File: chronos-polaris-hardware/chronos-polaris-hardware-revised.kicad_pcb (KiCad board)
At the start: 2 copper layers, 30 x 50 mm, 102 parts, among them J1 Conn_01x03_Pin, J2 Conn_01x03_Pin, J3 Conn_01x03_Pin, J4 Conn_01x03_Pin, J5 Conn_01x03_Pin, J6 Conn_01x04, J7 Conn_01x04, J8 Conn_01x02, J9 691417320006S, P1 WJ124-3_81-6P, Q1 US6K4TR, U1 TLV62130RGTR, U1 TPS62172DSGR, U10 MSK12C02-HB, U11 TPS62172DSGR, U12 AP20P30Q, U14 FC-B1010RGBT-HG, U15 TYPE-C_14PLC-H10_0, U2 ESP32-S2-SOLO-2-N4, U3 BMI088, U4 BMP280, U4 TYPE-C_14PLC-H10_0, U5 TF_PUSH, U6 TLV62130RGTR, U6 TPS629206DRLR, U7 AP20P30Q, U8 2N7002KDW_72K, U9 BMP280

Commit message: added footprint
footprint added for rigel connector. now all we need is to draw traces, layout, then ready for submit to jlcpcb
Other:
- board size 30 x 50 mm -> 40 x 50 mm

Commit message: fix merge conflicts . - Rishik B.
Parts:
- added BUZ1: HNB09A03, polaris-fp:BUZ-TH_BD9.0-P5.00-D0.6-FD, F.Cu at (188.8, 86.7)
- added C1: 22uF, Capacitor_SMD:C_0603_1608Metric, B.Cu at (212.1, 85.9)
- added C10: 100nF, Capacitor_SMD:C_0402_1005Metric, B.Cu at (194.1, 65.4)
- added C11: 3.3nF, Capacitor_SMD:C_0402_1005Metric, B.Cu at (194.4, 92.0)
- added C12: 100nF, Capacitor_SMD:C_0402_1005Metric, B.Cu at (189.4, 90.9)
- added C2: 10uF, Capacitor_SMD:C_0805_2012Metric, B.Cu at (212.2, 83.9)
- added C3: 22uF, Capacitor_SMD:C_0603_1608Metric, B.Cu at (188.8, 82.4)
- added C4: 10uF, Capacitor_SMD:C_0805_2012Metric, B.Cu at (191.4, 92.4)
- added C5: 100nF, Capacitor_SMD:C_0402_1005Metric, B.Cu at (194.1, 68.7)
- added C6: 100nF, Capacitor_SMD:C_0402_1005Metric, F.Cu at (197.1, 84.4)
- added C7: 100nF, Capacitor_SMD:C_0402_1005Metric, F.Cu at (197.1, 85.4)
- added C8: 100nF, Capacitor_SMD:C_0402_1005Metric, F.Cu at (205.6, 89.4)
- added C9: 100nF, Capacitor_SMD:C_0402_1005Metric, F.Cu at (205.6, 83.9)
- added H1: MountingHole, MountingHole:MountingHole_3.2mm_M3_Pad, F.Cu at (212.1, 101.4)
- added H4: MountingHole, MountingHole:MountingHole_3.2mm_M3_Pad, F.Cu at (187.6, 65.9)
- added J1: Conn_01x03_Pin, Connector_PinHeader_2.54mm:PinHeader_1x03_P2.54mm_Vertical, F.Cu at (187.1, 72.4)
- added J2: Conn_01x03_Pin, Connector_PinHeader_2.54mm:PinHeader_1x03_P2.54mm_Vertical, F.Cu at (187.1, 75.0)
- added J3: Conn_01x03_Pin, Connector_PinHeader_2.54mm:PinHeader_1x03_P2.54mm_Vertical, F.Cu at (187.1, 77.6)
- added J4: Conn_01x03_Pin, Connector_PinHeader_2.54mm:PinHeader_1x03_P2.54mm_Vertical, F.Cu at (187.1, 80.2)
- added J5: Conn_01x03_Pin, Connector_PinHeader_2.54mm:PinHeader_1x03_P2.54mm_Vertical, F.Cu at (186.0, 97.6)
- added J6: Conn_01x04, Connector_PinHeader_2.54mm:PinHeader_1x04_P2.54mm_Vertical, F.Cu at (186.0, 100.2)
- added J7: Conn_01x04, Connector_PinHeader_2.54mm:PinHeader_1x04_P2.54mm_Vertical, F.Cu at (186.0, 94.9)
- added J8: Conn_01x02, Connector_PinHeader_2.54mm:PinHeader_1x02_P2.54mm_Vertical, F.Cu at (192.6, 64.4)
- added J9: 691417320006S, polaris-fp:691417320006S, F.Cu at (202.5, 119.4)
- added L1: 2.2uH, polaris-fp:IND-SMD_L3.0-W3.0, B.Cu at (207.8, 89.2)
- added L2: 2.2uH, polaris-fp:IND-SMD_L4.0-W4.0, B.Cu at (192.6, 84.2)
- added R1: 100k, Resistor_SMD:R_0603_1608Metric, B.Cu at (206.6, 85.5)
- added R10: 51, Resistor_SMD:R_0603_1608Metric, B.Cu at (191.2, 70.2)
- added R11: 100, Resistor_SMD:R_0603_1608Metric, F.Cu at (191.3, 69.7)
- added R12: 0603WAF5101T5E, polaris-fp:R0603, B.Cu at (185.9, 111.7)
- added R13: 0603WAF5101T5E, polaris-fp:R0603, B.Cu at (188.8, 111.7)
- added R14: 30k, Resistor_SMD:R_0603_1608Metric, B.Cu at (208.0, 110.7)
- added R15: 10k, Resistor_SMD:R_0603_1608Metric, B.Cu at (208.1, 113.4)
- added R16: 10k, Resistor_SMD:R_0603_1608Metric, B.Cu at (198.9, 110.4)
- added R17: 30k, Resistor_SMD:R_0603_1608Metric, B.Cu at (193.1, 113.9)
- added R18: 10k, Resistor_SMD:R_0603_1608Metric, B.Cu at (192.8, 110.4)
- added R19: 100k, Resistor_SMD:R_0603_1608Metric, B.Cu at (197.1, 86.4)
- added R2: 10k, Resistor_SMD:R_0603_1608Metric, B.Cu at (196.1, 99.0)
- added R20: 160k, Resistor_SMD:R_0603_1608Metric, B.Cu at (195.6, 86.4)
- added R21: 10k, Resistor_SMD:R_0603_1608Metric, B.Cu at (189.6, 86.7)
- added R22: 30k, Resistor_SMD:R_0603_1608Metric, B.Cu at (209.9, 79.6)
- added R23: 10k, Resistor_SMD:R_0603_1608Metric, B.Cu at (209.9, 77.8)
- added R3: 10k, Resistor_SMD:R_0603_1608Metric, B.Cu at (202.6, 100.9)
- added R4: 10k, Resistor_SMD:R_0603_1608Metric, B.Cu at (199.1, 100.9)
- added R5: 10k, Resistor_SMD:R_0603_1608Metric, B.Cu at (199.1, 106.7)
- added R6: 10k, Resistor_SMD:R_0603_1608Metric, B.Cu at (202.4, 110.4)
- added R7: 30k, Resistor_SMD:R_0603_1608Metric, B.Cu at (195.6, 89.6)
- added R8: 10k, Resistor_SMD:R_0603_1608Metric, B.Cu at (191.8, 68.7)
- added R9: 51, Resistor_SMD:R_0603_1608Metric, B.Cu at (185.8, 70.2)
- added U1: TPS62172DSGR, polaris-fp:WSON-8_L2.0-W2.0-P0.50-TL-EP, B.Cu at (208.8, 85.4)
- added U10: MSK12C02-HB, polaris-fp:SW-TH_MSK12C02-HB-1, F.Cu at (210.2, 89.0)
- added U12: AP20P30Q, polaris-fp:DFN-8_L3.3-W3.0-P0.65-LS3.3-BL-EP, B.Cu at (203.1, 104.7)
- added U14: FC-B1010RGBT-HG, polaris-fp:LED-ARRAY-SMD_4P-L1.0-W1.0-TR-RD, F.Cu at (188.3, 70.0)
- added U15: TYPE-C_14PLC-H10_0, polaris-fp:USB-C-TH_SHOUHAN_TYPE-C-14PLC-H10.0, F.Cu at (187.1, 107.0)
- added U2: ESP32-S2-SOLO-2-N4, polaris-fp:WIRELM-SMD_ESP32-S3-WROOM-1, F.Cu at (203.9, 73.3)
- added U3: BMI088, polaris-fp:LGA-16_L4.5-W3.0-P0.50-BL, F.Cu at (204.6, 86.6)
- added U4: BMP280, polaris-fp:LGA-8_L2.5-W2.0-P0.65_AMP6127, F.Cu at (199.6, 85.4)
- added U5: TF_PUSH, polaris-fp:TF-SMD_TF-PUSH, B.Cu at (203.5, 70.9)
- added U6: TLV62130RGTR, polaris-fp:QFN-16_L3.0-W3.0-P0.50-TL-EP, B.Cu at (192.6, 89.2)
- added U7: AP20P30Q, polaris-fp:DFN-8_L3.3-W3.0-P0.65-LS3.3-BL-EP, B.Cu at (195.3, 104.7)
- added U8: 2N7002KDW_72K, polaris-fp:SOT-363_L2.1-W1.3-P0.65-LS2.3-BL, B.Cu at (199.1, 103.9)
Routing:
- net 3.3V: track 153.2 -> 291.2 mm, vias 11 -> 22
- net /BAT+: track 68.8 -> 148.7 mm, vias 1 -> 2
- net Net-(J6-Pin_2): track 59.9 -> 119.9 mm, vias 2 -> 4
- net /DROGUE DETECT: track 54.7 -> 112.6 mm, vias 3 -> 6
- net Net-(J7-Pin_1): track 57.5 -> 115.0 mm, vias 2 -> 4
- net GND: track 52.7 -> 105.4 mm, vias 46 -> 92
- net /MAIN DETECT: track 48.3 -> 98.5 mm, vias 3 -> 6
- net 5V: track 46.3 -> 92.5 mm
- net /MAIN CTRL: track 45.0 -> 90.1 mm, vias 5 -> 10
- net /USB_5V: track 43.2 -> 86.4 mm
- net Net-(J6-Pin_4): track 42.7 -> 85.5 mm, vias 3 -> 6
- net /DROGUE CTRL: track 39.7 -> 79.4 mm, vias 3 -> 6
- net Net-(U2-IO19): track 38.5 -> 77.0 mm
- net /GPIO0 (BOOTLOADER): track 37.6 -> 75.2 mm, vias 1 -> 2
- net Net-(U2-IO20): track 36.8 -> 73.5 mm, vias 1 -> 2
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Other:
- board size 40 x 50 mm -> 116.1 x 87.6 mm

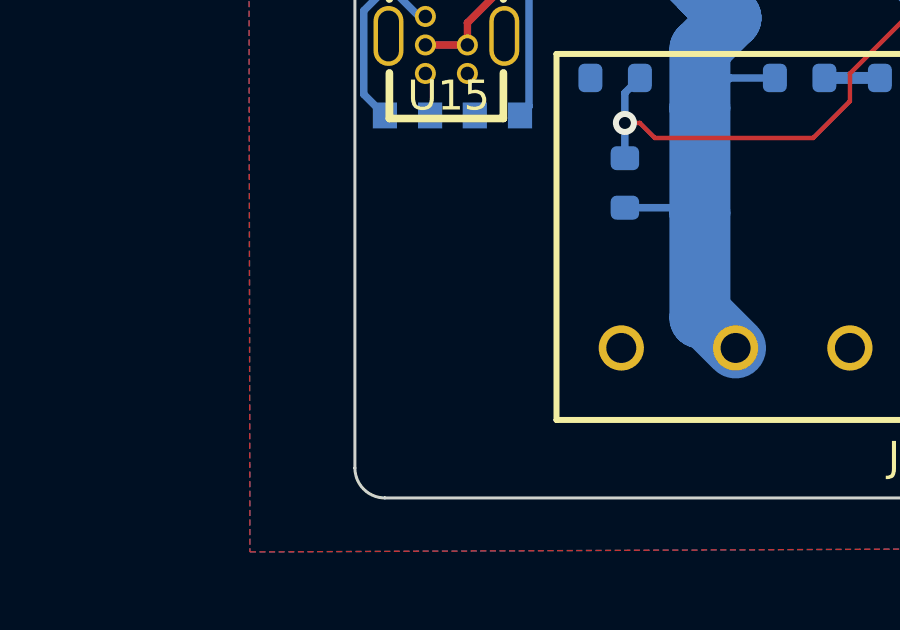
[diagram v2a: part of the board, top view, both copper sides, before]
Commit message: added the mount to board (no connecitons yet)
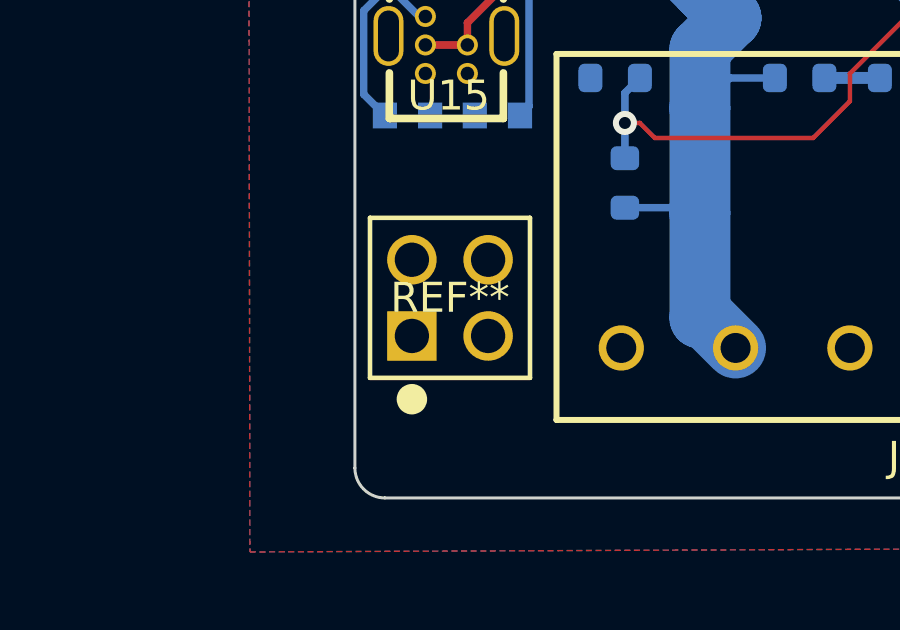
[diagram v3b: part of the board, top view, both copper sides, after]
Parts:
- added REF**: TSW-102-07-G-D_SAI, polaris-fp:TSW-102-07-G-D_SAI, F.Cu at (186.0, 119.0)

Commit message: PCB should be done with some minor design problems maybe - Rishik B
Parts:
- removed the BUZ1 at (188.8, 86.7)
- removed the BUZ1 at (104.8, 124.2)
- removed the C1 at (10.7, 0.48)
- removed the C1 at (128.0, 123.5)
- removed the C1 at (212.1, 85.9)
- removed the C10 at (110.0, 103.0)
- removed the C10 at (194.1, 65.4)
- removed the C11 at (1.50, 3.27)
- removed the C11 at (194.4, 92.0)
- removed the C11 at (110.3, 129.6)
- removed the C12 at (5.74, 14.7)
- removed the C12 at (189.4, 90.9)
- removed the C12 at (105.3, 128.5)
- removed the C2 at (5.74, 11.7)
- removed the C2 at (128.1, 121.5)
- removed the C2 at (212.2, 83.9)
- removed the C3 at (10.7, 2.46)
- removed the C3 at (188.8, 82.4)
- removed the C3 at (104.8, 120.0)
- removed the C4 at (1.50, 0.76)
- removed the C4 at (107.3, 130.0)
- removed the C4 at (191.4, 92.4)
- removed the C5 at (194.1, 68.7)
- removed the C5 at (110.0, 106.3)
- removed the C6 at (27.6, 6.07)
- removed the C6 at (197.1, 84.4)
- removed the C6 at (113.0, 122.0)
- removed the C7 at (113.0, 123.0)
- removed the C7 at (23.4, 0.76)
- removed the C7 at (197.1, 85.4)
- removed the C8 at (121.5, 127.0)
- removed the C8 at (205.6, 89.4)
- removed the C9 at (205.6, 83.9)
- removed the C9 at (121.5, 121.5)
- removed the H1 at (126.5, 138.5)
- removed the H1 at (212.1, 101.4)
- removed the H4 at (103.5, 103.5)
- removed the H4 at (187.6, 65.9)
- removed the J1 at (187.1, 72.4)
- removed the J1 at (103.0, 110.0)
- removed the J2 at (187.1, 75.0)
- removed the J2 at (103.0, 112.6)
- removed the J3 at (187.1, 77.6)
- removed the J3 at (103.0, 115.2)
- removed the J4 at (187.1, 80.2)
- removed the J4 at (103.0, 117.8)
- removed the J5 at (101.9, 135.2)
- removed the J5 at (186.0, 97.6)
- removed the J6 at (101.9, 137.8)
- removed the J6 at (186.0, 100.2)
- removed the J7 at (101.9, 132.5)
- removed the J7 at (186.0, 94.9)
- removed the J8 at (192.6, 64.4)
- removed the J8 at (108.5, 102.0)
- removed the J9 at (202.5, 119.4)
- removed the J9 at (13.1, 2.60)
- removed the L1 at (6.41, 2.17)
- removed the L1 at (123.7, 126.8)
- removed the L1 at (207.8, 89.2)
- removed the L2 at (6.41, 7.51)
- removed the L2 at (192.6, 84.2)
- removed the L2 at (108.5, 121.8)
- removed P1: WJ124-3_81-6P, polaris-fp:CONN-TH_6P-P3.81_WJ124-3.81-6P
- removed the R1 at (1.50, 5.78)
- removed the R1 at (206.6, 85.5)
- removed the R1 at (122.5, 123.1)
- removed the R10 at (191.2, 70.2)
- removed the R10 at (107.1, 107.8)
- removed the R11 at (191.3, 69.7)
- removed the R11 at (107.2, 107.2)
- removed the R12 at (1.50, 27.9)
- removed the R12 at (185.9, 111.7)
- removed the R12 at (101.8, 149.2)
- removed the R13 at (1.50, 30.4)
- removed the R13 at (104.8, 149.2)
- removed the R13 at (188.8, 111.7)
- removed the R14 at (17.3, 26.1)
- removed the R14 at (123.9, 148.2)
- removed the R14 at (208.0, 110.7)
- removed R15 (x2), R16 (x2), R18 (x2): 10k, Resistor_SMD:R_0603_1608Metric
- removed R17 (x2): 30k, Resistor_SMD:R_0603_1608Metric
- removed the R19 at (1.50, 15.8)
- removed the R19 at (197.1, 86.4)
- removed the R19 at (113.0, 124.0)
- removed the R2 at (1.50, 8.29)
- removed the R2 at (196.1, 99.0)
- removed the R2 at (112.0, 136.6)
- removed the R20 at (1.50, 18.3)
- removed the R20 at (111.5, 124.0)
- removed the R20 at (195.6, 86.4)
- removed the R21 at (17.4, 0.76)
- removed the R21 at (189.6, 86.7)
- removed the R21 at (105.5, 124.3)
- removed the R22 at (17.4, 3.27)
- removed the R22 at (125.8, 117.2)
- removed the R22 at (209.9, 79.6)
- removed the R23 at (17.4, 5.78)
- removed the R23 at (209.9, 77.8)
- removed the R23 at (125.8, 115.4)
- removed the R3 at (1.50, 10.8)
- removed the R3 at (118.5, 138.5)
- removed the R3 at (202.6, 100.9)
- removed the R4 at (1.50, 22.8)
- removed the R4 at (199.1, 100.9)
- removed the R4 at (115.0, 138.5)
- removed the R5 at (1.50, 25.3)
- removed the R5 at (115.0, 144.2)
- removed the R5 at (199.1, 106.7)
- removed the R6 at (17.3, 23.6)
- removed the R6 at (120.8, 148.2)
- removed the R6 at (202.4, 110.4)
- removed the R7 at (1.50, 13.3)
- removed the R7 at (195.6, 89.6)
- removed the R7 at (111.5, 127.2)
- removed the R8 at (107.8, 106.2)
- removed the R8 at (191.8, 68.7)
- removed the R9 at (185.8, 70.2)
- removed the R9 at (101.7, 107.8)
- removed REF**: TSW-102-07-G-D_SAI, polaris-fp:TSW-102-07-G-D_SAI
- removed the U1 at (11.0, 12.6)
- removed the U1 at (208.8, 85.4)
- removed the U1 at (124.8, 123.0)
- removed the U10 at (210.2, 89.0)
- removed the U10 at (126.1, 126.6)
- removed U12 (x2), U7 (x2): AP20P30Q, polaris-fp:DFN-8_L3.3-W3.0-P0.65-LS3.3-BL-EP
- removed the U14 at (104.2, 107.6)
- removed the U14 at (188.3, 70.0)
- removed U15 (x2): TYPE-C_14PLC-H10_0, polaris-fp:USB-C-TH_SHOUHAN_TYPE-C-14PLC-H10.0
- removed the U2 at (119.8, 110.9)
- removed the U2 at (203.9, 73.3)
- removed the U3 at (204.6, 86.6)
- removed the U3 at (120.5, 124.2)
- removed the U4 at (199.6, 85.4)
- removed the U4 at (20.8, 19.5)
- removed the U4 at (115.5, 123.0)
- removed the U5 at (119.4, 108.5)
- removed the U5 at (203.5, 70.9)
- removed the U6 at (10.3, 16.9)
- removed the U6 at (108.5, 126.8)
- removed the U6 at (192.6, 89.2)
- removed U8 (x2): 2N7002KDW_72K, polaris-fp:SOT-363_L2.1-W1.3-P0.65-LS2.3-BL
- added BUZ1: HNB09A03, polaris-fp:BUZ-TH_BD9.0-P5.00-D0.6-FD, F.Cu at (76.5, 71.5)
- added C1: 100nF, Capacitor_SMD:C_0402_1005Metric, B.Cu at (89.5, 96.5)
- added C10: 100nF, Capacitor_SMD:C_0402_1005Metric, B.Cu at (93.7, 98.0)
- added C11: 22uF, Capacitor_SMD:C_0603_1608Metric, F.Cu at (89.8, 88.0)
- added C12: 4.7uF, Capacitor_SMD:C_0805_2012Metric, F.Cu at (82.5, 78.0)
- added C2: 10uF, Capacitor_SMD:C_0805_2012Metric, B.Cu at (89.5, 94.5)
- added C3: 3.3nF, Capacitor_SMD:C_0402_1005Metric, F.Cu at (96.5, 81.0)
- added C4: 22uF, Capacitor_SMD:C_0603_1608Metric, F.Cu at (90.0, 86.5)
- added C5: 100nF, Capacitor_SMD:C_0402_1005Metric, F.Cu at (80.0, 57.5)
- added C6: 10uF, Capacitor_SMD:C_0805_2012Metric, F.Cu at (78.0, 85.5)
- added C7: 22uF, Capacitor_SMD:C_0603_1608Metric, B.Cu at (93.2, 94.5)
- added C8: 100nF, Capacitor_SMD:C_0402_1005Metric, B.Cu at (93.7, 96.0)
- added C9: 100nF, Capacitor_SMD:C_0402_1005Metric, B.Cu at (93.7, 97.0)
- added H1: MountingHole, MountingHole:MountingHole_3.2mm_M3_Pad, F.Cu at (103.5, 100.5)
- added H4: MountingHole, MountingHole:MountingHole_3.2mm_M3_Pad, F.Cu at (76.5, 52.5)
- added J1: Conn_01x03_Pin, Connector_PinHeader_2.54mm:PinHeader_1x03_P2.54mm_Vertical, F.Cu at (99.0, 81.0)
- added J10: TSW-102-07-G-D, polaris-fp:TSW-102-07-G-D_SAI, F.Cu at (74.0, 64.5)
- added J2: Conn_01x03_Pin, Connector_PinHeader_2.54mm:PinHeader_1x03_P2.54mm_Vertical, F.Cu at (102.0, 81.0)
- added J3: Conn_01x03_Pin, Connector_PinHeader_2.54mm:PinHeader_1x03_P2.54mm_Vertical, F.Cu at (101.0, 90.0)
- added J4: Conn_01x03_Pin, Connector_PinHeader_2.54mm:PinHeader_1x03_P2.54mm_Vertical, F.Cu at (97.5, 95.0)
- added J5: Conn_01x03_Pin, Connector_PinHeader_2.54mm:PinHeader_1x03_P2.54mm_Vertical, F.Cu at (105.0, 90.0)
- added J6: Conn_01x04, Connector_PinHeader_2.54mm:PinHeader_1x04_P2.54mm_Vertical, F.Cu at (105.0, 78.4)
- added J7: Conn_01x04, Connector_PinHeader_2.54mm:PinHeader_1x04_P2.54mm_Vertical, F.Cu at (105.0, 67.4)
- added J8: Conn_01x02, Connector_PinHeader_2.54mm:PinHeader_1x02_P2.54mm_Vertical, F.Cu at (73.7, 59.0)
- added J9: 691417320006S, polaris-fp:691417320006S, F.Cu at (82.5, 99.0)
- added L1: 2.2uH, polaris-fp:IND-SMD_L4.0-W4.0, F.Cu at (93.5, 86.5)
- added L2: 2.2uH, polaris-fp:IND-SMD_L4.0-W4.0, F.Cu at (89.0, 83.0)
- added R1: 10k, Resistor_SMD:R_0603_1608Metric, F.Cu at (99.5, 77.5)
- added R10: 51, Resistor_SMD:R_0603_1608Metric, F.Cu at (102.5, 62.0)
- added R11: 100, Resistor_SMD:R_0603_1608Metric, F.Cu at (102.5, 60.5)
- added R12: ?, Resistor_SMD:R_0603_1608Metric, F.Cu at (80.7, 85.0)
- added R13: ?, Resistor_SMD:R_0603_1608Metric, F.Cu at (80.8, 86.5)
- added R14: 0603WAF5101T5E, polaris-fp:R0603, B.Cu at (81.8, 83.5)
- added R19: 30k, Resistor_SMD:R_0603_1608Metric, B.Cu at (85.5, 90.5)
- added R2: 240k, Resistor_SMD:R_0603_1608Metric, F.Cu at (87.5, 77.0)
- added R20: 100k, Resistor_SMD:R_0603_1608Metric, F.Cu at (89.0, 79.5)
- added R21: 10k, Resistor_SMD:R_0603_1608Metric, B.Cu at (84.8, 94.5)
- added R22: 30k, Resistor_SMD:R_0603_1608Metric, B.Cu at (73.5, 83.5)
- added R23: 10k, Resistor_SMD:R_0603_1608Metric, B.Cu at (74.0, 71.5)
- added R3: 27.4k, Resistor_SMD:R_0603_1608Metric, F.Cu at (92.5, 77.0)
- added R4: 10k, Resistor_SMD:R_0603_1608Metric, F.Cu at (80.0, 60.5)
- added R5: 10k, Resistor_SMD:R_0603_1608Metric, F.Cu at (80.0, 62.0)
- added R6: 0603WAF5101T5E, polaris-fp:R0603, F.Cu at (82.2, 83.5)
- added R7: 160k, Resistor_SMD:R_0603_1608Metric, F.Cu at (95.3, 83.5)
- added R8: 10k, Resistor_SMD:R_0603_1608Metric, F.Cu at (80.0, 59.0)
- added R9: 51, Resistor_SMD:R_0603_1608Metric, F.Cu at (102.5, 63.5)
- added U1: TLV62130RGTR, polaris-fp:QFN-16_L3.0-W3.0-P0.50-TL-EP, F.Cu at (93.7, 80.7)
- added U10: MSK12C02-HB, polaris-fp:SW-TH_MSK12C02-HB-1, F.Cu at (85.0, 82.5)
- added U14: FC-B1010RGBT-HG, polaris-fp:LED-ARRAY-SMD_4P-L1.0-W1.0-TR-RD, F.Cu at (104.8, 61.5)
- added U2: ESP32, polaris-fp:WIRELM-SMD_ESP32-S3-WROOM-1, F.Cu at (91.2, 65.9)
- added U3: BMI088, polaris-fp:LGA-16_L4.5-W3.0-P0.50-BL, B.Cu at (94.1, 72.0)
- added U4: TYPE-C_14PLC-H10_0, polaris-fp:USB-C-TH_SHOUHAN_TYPE-C-14PLC-H10.0, F.Cu at (76.5, 79.6)
- added U5: TF_PUSH, polaris-fp:TF-SMD_TF-PUSH, B.Cu at (90.5, 63.9)
- added U6: TPS629206DRLR, footprints:SOT5X3-8_DRL_TEX, F.Cu at (90.0, 77.0)
- C13, L3, R24, R26, R27, R28, U11, U9: moved to B.Cu
- moved R27 105.0 mm to (82.0, 91.0), turned to 180 degrees
- moved L3 101.3 mm to (91.5, 81.0)
- moved R25 101.0 mm to (101.5, 69.8), turned to 90 degrees
- moved R28 99.5 mm to (77.0, 90.5), turned to 180 degrees
- moved R24 92.2 mm to (84.5, 72.3), turned to 90 degrees
- moved Q1 92.0 mm to (74.5, 85.8), turned to 90 degrees
- moved U9 91.8 mm to (96.0, 78.3), turned to -90 degrees
- moved U11 88.7 mm to (85.0, 77.0)
- moved R26 88.6 mm to (80.0, 76.5), turned to 180 degrees
- moved C13 87.6 mm to (97.0, 73.0), turned to 90 degrees
- moved C14 87.3 mm to (98.0, 72.5), turned to 90 degrees
- moved R29 81.2 mm to (80.0, 65.0), turned to 180 degrees
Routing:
- net Net-(J7-Pin_1): track 115.0 -> 9.36 mm, vias 4 -> 2
- net GND: track 105.4 -> 1.40 mm, vias 92 -> 0
- net Net-(J6-Pin_2): track 119.9 -> 25.3 mm, vias 4 -> 0
- net /BAT+: track 148.7 -> 55.4 mm
- net 3.3V: track 291.2 -> 199.0 mm, vias 22 -> 10
- net /MAIN CTRL: track 90.1 -> 0.00 mm, vias 10 -> 0
- net /DROGUE CTRL: track 79.4 -> 0.00 mm, vias 6 -> 0
- net Net-(U2-IO19): track 77.0 -> 0.00 mm
- net Net-(U2-IO20): track 73.5 -> 0.00 mm, vias 2 -> 0
- net /MAIN DETECT: track 98.5 -> 29.4 mm, vias 6 -> 4
- net 5V_ENABLE: track 68.3 -> 0.00 mm, vias 2 -> 0
- net /USB_5V: track 86.4 -> 22.1 mm
- net /DROGUE DETECT: track 112.6 -> 50.3 mm, vias 6 -> 0
- net Net-(U2-IO42): track 57.2 -> 1.77 mm, vias 2 -> 0
- net VIN_1/4: track 8.85 -> 63.4 mm, vias 2 -> 1
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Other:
- board outline removed
- board text removed: "+"
- board text removed: "-"
- board text removed: "3.5-13V"
- board text removed: "3v3"
- board text removed: "5v"
- board text removed: "C1"
- board text removed: "C2"
- board text removed: "CHRONOS ROCKETRY"
- board text removed: "CS SPICLK SDI SDO"
- board text removed: "G/5/3V3"
- board text removed: "G/IO1/3V3/IO2"
- board text removed: "GND"
- board text removed: "LONGHORN ROCKETRY"
- board text removed: "POLARIS"
- board text removed: "REV 1 FC"
- board text removed: "S"
- board text removed: "VIN"

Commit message: updated border. - Rishik B.
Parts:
- moved H1 3.00 mm to (100.5, 100.5)
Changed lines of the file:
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@@
 	(footprint "MountingHole:MountingHole_3.2mm_M3_Pad"
 		(layer "F.Cu")
-		(at 103.5 100.5)
+		(at 100.5 100.5)
 		(descr "Mounting Hole 3.2mm, M3")
 		(tags "mounting hole 3.2mm m3")
@@
 		)
 	)
+	(gr_rect
+		(start 70 48.5)
+		(end 106 105.7)
+		(stroke
+			(width 0.2)
+			(type default)
+		)
+		(fill none)
+		(layer "F.Cu")
+	)
 	(segment
 		(start 73.249809 80.270129)
@@
 		(min_thickness 0.25)
 		(filled_areas_thickness no)
-		(fill yes
+		(fill
 			(thermal_gap 0.5)
 			(thermal_bridge_width 0.5)
@@
 		(polygon
 			(pts
-				(xy 106.5 48.7) (xy 70 48.5) (xy 69.1 105.9) (xy 106 105.7)
+				(xy 106 48.5) (xy 70 48.5) (xy 70 105.7) (xy 106 105.7)
 			)
 		)
